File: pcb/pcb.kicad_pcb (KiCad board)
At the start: 2 copper layers, 72.1 x 36.1 mm, 30 parts, among them J1 USB_C_Receptacle_USB2.0_16P, J3 Conn_01x02_MountingPin, J4 Conn_02x03_Odd_Even, SW1 SW_SPDT, SW2 RST, SW3 Kailh_Choc, SW4 Kailh_Choc, SW5 Kailh_Choc, SW6 Kailh_Choc, SW7 Kailh_Choc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

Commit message: small changes to pcb, also did some bom
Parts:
- moved R6 0.19 mm to (47.8, 90.7), turned to 0 degrees
- moved R5 0.10 mm to (47.8, 92.2), turned to 180 degrees
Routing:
- net +5V: track 95.2 -> 85.8 mm
- net /USB-D+: track 20.6 -> 15.9 mm
- net GND: track 15.4 -> 12.3 mm, vias 3 -> 5
- net /VSENSE: track 6.11 -> 4.23 mm

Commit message: case
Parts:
- SW2: moved to B.Cu
- moved SW1 1.75 mm to (31.1, 76.1)
- moved SW2 1.30 mm to (30.3, 83.4), turned to -90 degrees
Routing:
- net GND: track 12.3 -> 15.1 mm, vias 5 -> 6
- net /RST: track 25.6 -> 23.3 mm, vias 3 -> 2
- net +BATT: track 28.3 -> 29.7 mm
- net Net-(J3-Pin_1): track 70.1 -> 69.4 mm
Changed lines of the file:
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@@
 		)
 	)
-	(footprint "horrortroll_lib:TS-1088R-02526"
-		(layer "F.Cu")
-		(at 30.425 84.7 90)
-		(property "Reference" "SW2"
-			(at 0 0 90)
-			(layer "F.SilkS")
-			(effects
-				(font
-					(size 1 1)
-					(thickness 0.15)
-				)
-			)
-		)
-		(property "Value" "RST"
-			(at 0 2.2 90)
-			(layer "F.Fab")
-			(effects
-				(font
-					(size 1 1)
-					(thickness 0.15)
-				)
-			)
-		)
-		(property "Datasheet" ""
-			(at 0 0 90)
-			(layer "F.Fab")
-			(hide yes)
-			(effects
-				(font
-					(size 1.27 1.27)
-					(thickness 0.15)
-				)
-			)
-		)
-		(property "Description" "Push button switch, normally open, two pins, 45° tilted"
-			(at 0 0 90)
-			(layer "F.Fab")
-			(hide yes)
-			(effects
-				(font
-					(size 1.27 1.27)
-					(thickness 0.15)
-				)
-			)
-		)
-		(sheetname "/")
-		(sheetfile "pcb.kicad_sch")
-		(attr through_hole)
-		(fp_line
-			(start -1.9 -1.2)
-			(end 1.9 -1.2)
-			(stroke
-				(width 0.12)
-				(type solid)
-			)
-			(layer "F.SilkS")
-		)
-		(fp_line
-			(start 1.9 1.2)
-			(end -1.9 1.2)
-			(stroke
-				(width 0.12)
-				(type solid)
-			)
-			(layer "F.SilkS")
-		)
-		(pad "1" smd rect
-			(at -2.225 0 90)
-			(size 1.05 2)
-			(layers "F.Cu" "F.Mask" "F.Paste")
-			(net 16 "/RST")
-			(pinfunction "1")
-			(pintype "passive")
-		)
-		(pad "2" smd rect
-			(at 2.225 0 90)
-			(size 1.05 2)
-			(layers "F.Cu" "F.Mask" "F.Paste")
-			(net 1 "GND")
-			(pinfunction "2")
-			(pintype "passive")
-		)
-		(embedded_fonts no)
-		(model "${KICAD6_3DMODEL_DIR}/Button_Switch_SMD.3dshapes/SW_SPST_B3U-1000P.step"
-			(offset
-				(xyz 0 0 0)
-			)
-			(scale
-				(xyz 1 1 1)
-			)
-			(rotate
-				(xyz 0 0 0)
-			)
-		)
-	)
 	(footprint "PCM_marbastlib-various:nRF52840_holyiot_18010"
 		(layer "F.Cu")
@@
 		)
 	)
+	(footprint "horrortroll_lib:TS-1088R-02526"
+		(layer "B.Cu")
+		(at 30.325 83.4 -90)
+		(property "Reference" "SW2"
+			(at 0 0 90)
+			(layer "B.SilkS")
+			(effects
+				(font
+					(size 1 1)
+					(thickness 0.15)
+				)
+				(justify mirror)
+			)
+		)
+		(property "Value" "RST"
+			(at 0 -2.2 90)
+			(layer "B.Fab")
+			(effects
+				(font
+					(size 1 1)
+					(thickness 0.15)
+				)
+				(justify mirror)
+			)
+		)
+		(property "Datasheet" ""
+			(at 0 0 90)
+			(layer "B.Fab")
+			(hide yes)
+			(effects
+				(font
+					(size 1.27 1.27)
+					(thickness 0.15)
+				)
+				(justify mirror)
+			)
+		)
+		(property "Description" "Push button switch, normally open, two pins, 45° tilted"
+			(at 0 0 90)
+			(layer "B.Fab")
+			(hide yes)
+			(effects
+				(font
+					(size 1.27 1.27)
+					(thickness 0.15)
+				)
+				(justify mirror)
+			)
+		)
+		(sheetname "/")
+		(sheetfile "pcb.kicad_sch")
+		(attr through_hole)
+		(fp_line
+			(start -1.9 1.2)
+			(end 1.9 1.2)
+			(stroke
+				(width 0.12)
+				(type solid)
+			)
+			(layer "B.SilkS")
+		)
+		(fp_line
+			(start 1.9 -1.2)
+			(end -1.9 -1.2)
+			(stroke
+				(width 0.12)
+				(type solid)
+			)
+			(layer "B.SilkS")
+		)
+		(pad "1" smd rect
+			(at -2.225 0 270)
+			(size 1.05 2)
+			(layers "B.Cu" "B.Mask" "B.Paste")
+			(net 16 "/RST")
+			(pinfunction "1")
+			(pintype "passive")
+		)
+		(pad "2" smd rect
+			(at 2.225 0 270)
+			(size 1.05 2)
+			(layers "B.Cu" "B.Mask" "B.Paste")
+			(net 1 "GND")
+			(pinfunction "2")
+			(pintype "passive")
+		)
+		(embedded_fonts no)
+		(model "${KICAD6_3DMODEL_DIR}/Button_Switch_SMD.3dshapes/SW_SPST_B3U-1000P.step"
+			(offset
+				(xyz 0 0 0)
+			)
+			(scale
+				(xyz 1 1 1)
+			)
+			(rotate
+				(xyz 0 0 0)
+			)
+		)
+	)
 	(footprint "Resistor_SMD:R_0603_1608Metric"
 		(layer "B.Cu")
@@
 	(footprint "Button_Switch_SMD:SW_SPDT_PCM12"
 		(layer "B.Cu")
-		(at 32.77 76.75 90)
+		(at 31.14 76.12 90)
 		(descr "Ultraminiature Surface Mount Slide Switch, right-angle, https://www.ckswitches.com/media/1424/pcm.pdf")
 		(property "Reference" "SW1"
@@
 		(net 1)
 	)
+	(via
+		(at 31.675 83.35)
+		(size 0.6)
+		(drill 0.3)
+		(layers "F.Cu" "B.Cu")
+		(net 1)
+	)
+	(segment
+		(start 30.325 85.625)
+		(end 30.325 84.7)
+		(width 0.38)
+		(layer "B.Cu")
+		(net 1)
+	)
 	(segment
 		(start 47.9 78.25)
@@
 	)
 	(segment
+		(start 30.325 84.7)
+		(end 31.675 83.35)
+		(width 0.38)
+		(layer "B.Cu")
+		(net 1)
+	)
+	(segment
 		(start 47.92 77.295)
 		(end 47.9 77.275)
@@
 	)
 	(segment
+		(start 34.83 73.87)
+		(end 32.57 73.87)
+		(width 0.38)
+		(layer "B.Cu")
+		(net 3)
+	)
+	(segment
 		(start 35.956 72.744)
 		(end 57.899001 72.744)
@@
 	)
 	(segment
-		(start 34.2 74.5)
-		(end 35.956 72.744)
+		(start 59.985 73.485)
+		(end 58.640001 73.485)
 		(width 0.38)
 		(layer "B.Cu")
@@
 	)
 	(segment
-		(start 59.985 73.485)
-		(end 58.640001 73.485)
+		(start 34.83 73.87)
+		(end 35.956 72.744)
 		(width 0.38)
 		(layer "B.Cu")
@@
 		(net 16)
 	)
-	(segment
-		(start 30.525 84.775)
-		(end 30.425 84.875)
-		(width 0.2)
-		(layer "F.Cu")
-		(net 16)
-	)
-	(segment
-		(start 30.425 84.875)
-		(end 30.425 86.925)
-		(width 0.2)
-		(layer "F.Cu")
-		(net 16)
-	)
 	(via
 		(at 40.799 82.67053)
@@
 	)
 	(via
-		(at 30.525 84.775)
-		(size 0.6)
-		(drill 0.3)
-		(layers "F.Cu" "B.Cu")
-		(net 16)
-	)
-	(via
 		(at 36.7 87.025)
 		(size 0.6)
@@
 	)
 	(segment
-		(start 31.725 84.775)
-		(end 30.525 84.775)
+		(start 30.325 81.175)
+		(end 32.475 81.175)
 		(width 0.2)
 		(layer "B.Cu")
@@
 	)
 	(segment
-		(start 33.9 82.6)
-		(end 31.725 84.775)
+		(start 41.95 86.5)
+		(end 40.799 87.651)
 		(width 0.2)
 		(layer "B.Cu")
@@
 	)
 	(segment
-		(start 41.95 86.5)
-		(end 40.799 87.651)
+		(start 32.475 81.175)
+		(end 33.9 82.6)
 		(width 0.2)
 		(layer "B.Cu")
@@
 	)
 	(segment
-		(start 35.5 76.3)
-		(end 35.5 74.849936)
+		(start 62.625 72.75)
+		(end 37.51 72.75)
 		(width 0.38)
 		(layer "F.Cu")
@@
 	)
 	(segment
-		(start 63.85 73.975)
-		(end 63.85 82.275)
+		(start 37.51 72.75)
+		(end 34.89 75.37)
 		(width 0.38)
 		(layer "F.Cu")
@@
 	)
 	(segment
-		(start 63.85 82.275)
-		(end 63.3 82.825)
+		(start 63.3 82.825)
+		(end 63.85 82.275)
 		(width 0.38)
 		(layer "F.Cu")
@@
 	)
 	(segment
-		(start 62.625 72.75)
+		(start 63.85 82.275)
 		(end 63.85 73.975)
 		(width 0.38)
@@
 	)
 	(segment
-		(start 35.5 74.849936)
-		(end 37.599936 72.75)
-		(width 0.38)
-		(layer "F.Cu")
-		(net 18)
-	)
-	(segment
-		(start 37.599936 72.75)
+		(start 63.85 73.975)
 		(end 62.625 72.75)
 		(width 0.38)
@@
 	)
 	(via
-		(at 35.5 76.3)
+		(at 63.3 82.825)
 		(size 0.6)
 		(drill 0.3)
@@
 	)
 	(via
-		(at 63.3 82.825)
+		(at 34.89 75.37)
 		(size 0.6)
 		(drill 0.3)
@@
 	)
 	(segment
-		(start 34.2 76)
-		(end 34.6 76)
+		(start 32.57 75.37)
+		(end 34.89 75.37)
 		(width 0.38)
 		(layer "B.Cu")
@@
 		(width 0.38)
 		(layer "B.Cu")
-		(net 18)
-	)
-	(segment
-		(start 35.5 76.3)
-		(end 34.5 76.3)
-		(width 0.38)
-		(layer "B.Cu")
-		(net 18)
-	)
-	(segment
-		(start 34.25 75.975)
-		(end 33.66 75.975)
-		(width 0.38)
-		(layer "B.Cu")
-		(net 18)
-	)
-	(segment
-		(start 34.5 76.3)
-		(end 34.2 76)
-		(width 0.38)
-		(layer "B.Cu")

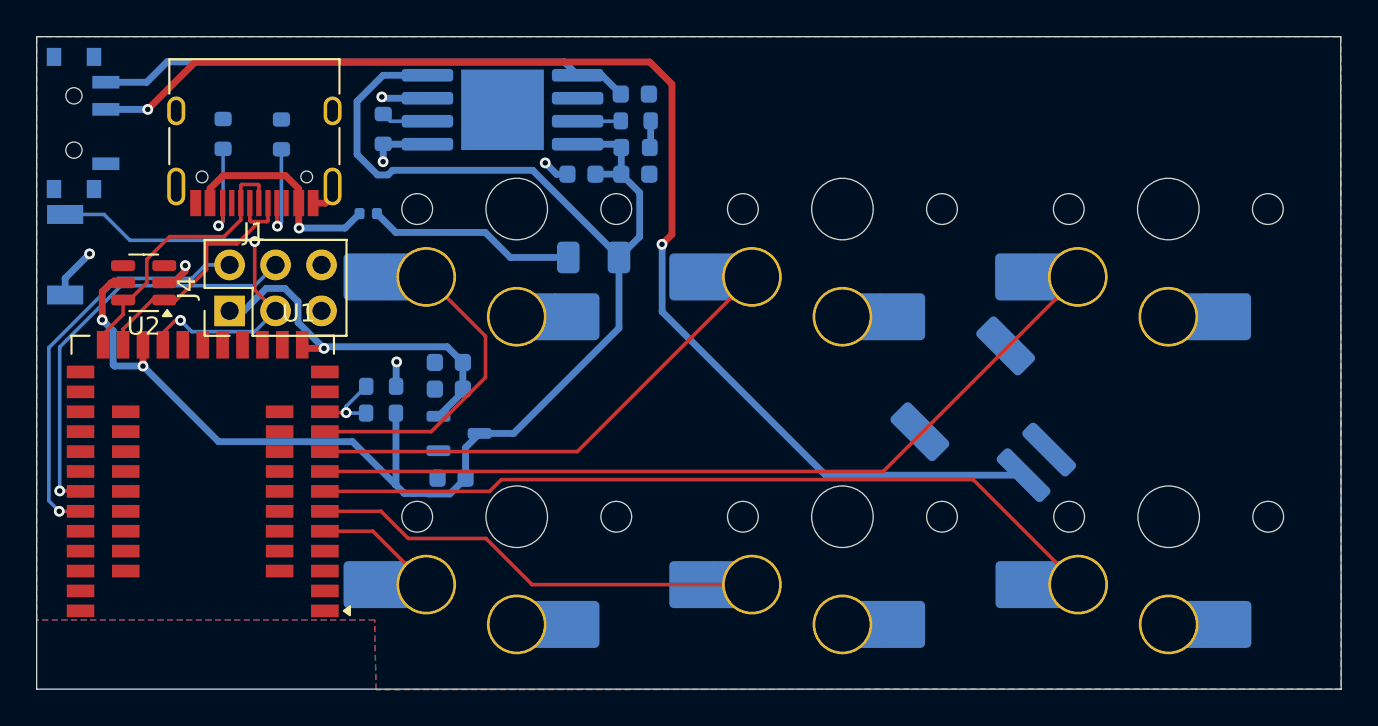
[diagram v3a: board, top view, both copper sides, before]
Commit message: firmware in zmk (wow that was hard)
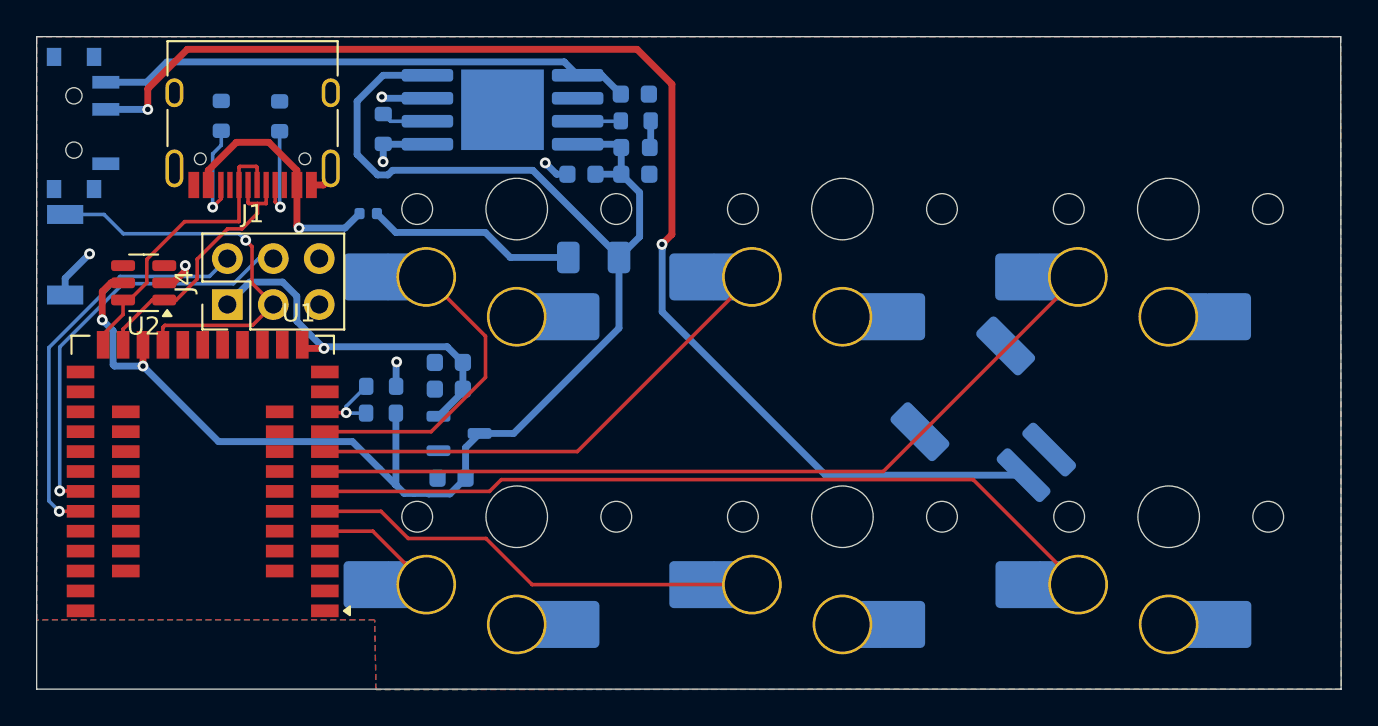
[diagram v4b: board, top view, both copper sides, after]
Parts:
- moved J1 1.00 mm to (40.7, 75.5)
- moved R2 1.00 mm to (42.2, 75.8)
- moved R1 1.00 mm to (39.0, 75.7)
- moved J4 0.37 mm to (39.3, 86.2)
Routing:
- net VBUS: track 12.1 -> 13.9 mm
- net Net-(J3-Pin_1): track 69.4 -> 70.6 mm
- net /RST: track 23.3 -> 22.3 mm, vias 2 -> 1
- net /USB-D+: track 15.9 -> 16.9 mm

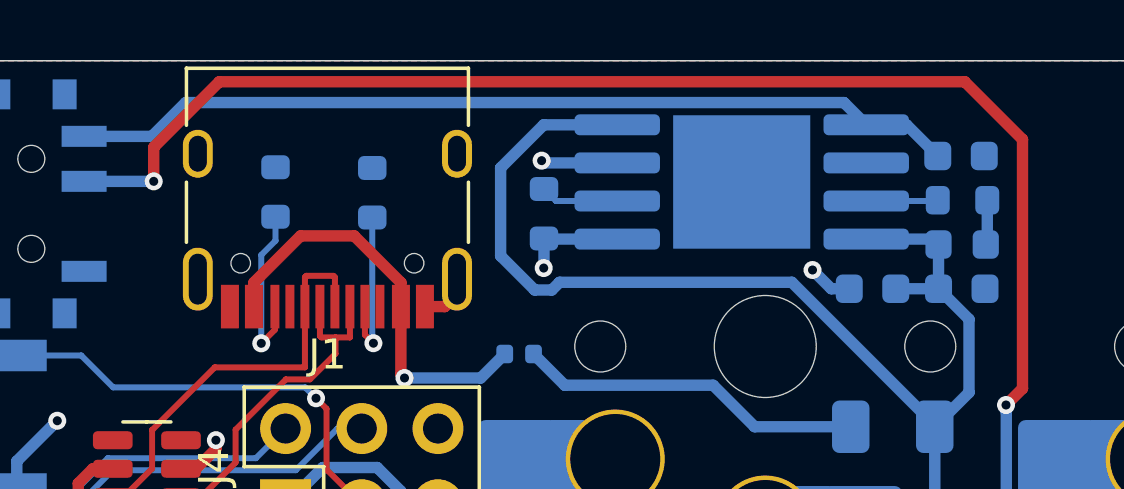
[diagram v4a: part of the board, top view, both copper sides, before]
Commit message: update tp4056 footprint
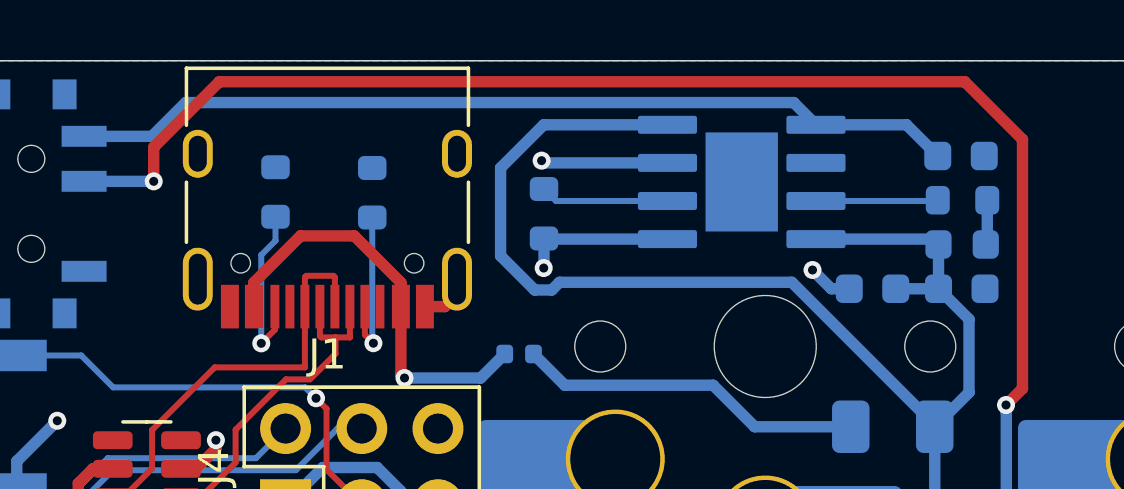
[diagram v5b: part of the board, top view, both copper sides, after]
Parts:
- U3: footprint Package_SO:SOP-8-1EP_4.57x4.57mm_P1.27mm_EP4.57x4.45mm -> TP4056:SOP127P600X175-9N
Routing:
- net +5V: track 85.8 -> 89.2 mm
- net GND: track 15.1 -> 18.5 mm
- net Net-(U3-PROG): track 2.61 -> 4.28 mm
- net Net-(U3-CHRG): track 2.40 -> 4.07 mm
